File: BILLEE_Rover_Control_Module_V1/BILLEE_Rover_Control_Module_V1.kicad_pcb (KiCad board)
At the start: 4 copper layers, 240 x 90.5 mm, 276 parts, among them CN1 XT90PW-M.G.Y, CN10 XT60PW-M, CN11 XT60PW-M, CN12 XT60PW-M, CN13 XT60PW-M, CN14 XT60PW-M, CN15 XT60PW-M, CN16 XT60PW-M, CN17 XT60PW-M, CN18 XT60PW-M, CN2 XT60PW-M, CN3 XT60PW-M, CN4 XT60PW-M, CN5 XT60PW-M, CN6 DF11-18DP-2DSA, CN7 XT90PW-M.G.Y, CN8 XT90PW-M.G.Y, CN9 XT90PW-M.G.Y, J1 2.54mm Header, Q1 IPT007N06N, Q2 IPT007N06N, Q3 IPT007N06N, Q4 IPT007N06N, Q5 IPT007N06N, Q6 IPT007N06N, Q7 IPT007N06N, Q8 IPT007N06N, SW1 33uH, SW2 KMR2, SW3 RESET SW, U1 INA780BIDEKR, U10 RP2350A_C42411118, U11 ABM8-272-T3_C20625731, U12 W25Q128JVSIQTR, U13 TCA4307DGKR, U14 TCA4307DGKR, U15 TXS0108EPWR, U16 ESTOP, U17 SN74LVC08APWR, U18 SN74LVC08APWR, U19 LTC7001IMSE#PBF, U2 MCP9808T-E/MS, U20 LTC7001IMSE#PBF, U21 LTC7001IMSE#PBF, U22 LTC7001IMSE#PBF, U23 LTC7001IMSE#PBF, U24 LTC7001IMSE#PBF, U25 INA780BIDEKR, U26 INA780BIDEKR, U27 INA780BIDEKR, U28 INA780BIDEKR, U29 INA780BIDEKR, U3 TPS1HA08BQPWPRQ1, U30 INA780BIDEKR, U31 LTC7001IMSE#PBF, U32 LTC7001IMSE#PBF, U33 INA780BIDEKR, U34 INA780BIDEKR, U35 MCP9808T-E/MS, U36 MCP9808T-E/MS, U4 TPS1HA08BQPWPRQ1, U5 TPS1HA08BQPWPRQ1, U6 LT8612EUDE#TRPBF, U7 LT8612EUDE#TRPBF, U8 LT8612EUDE#TRPBF, U9 10uH

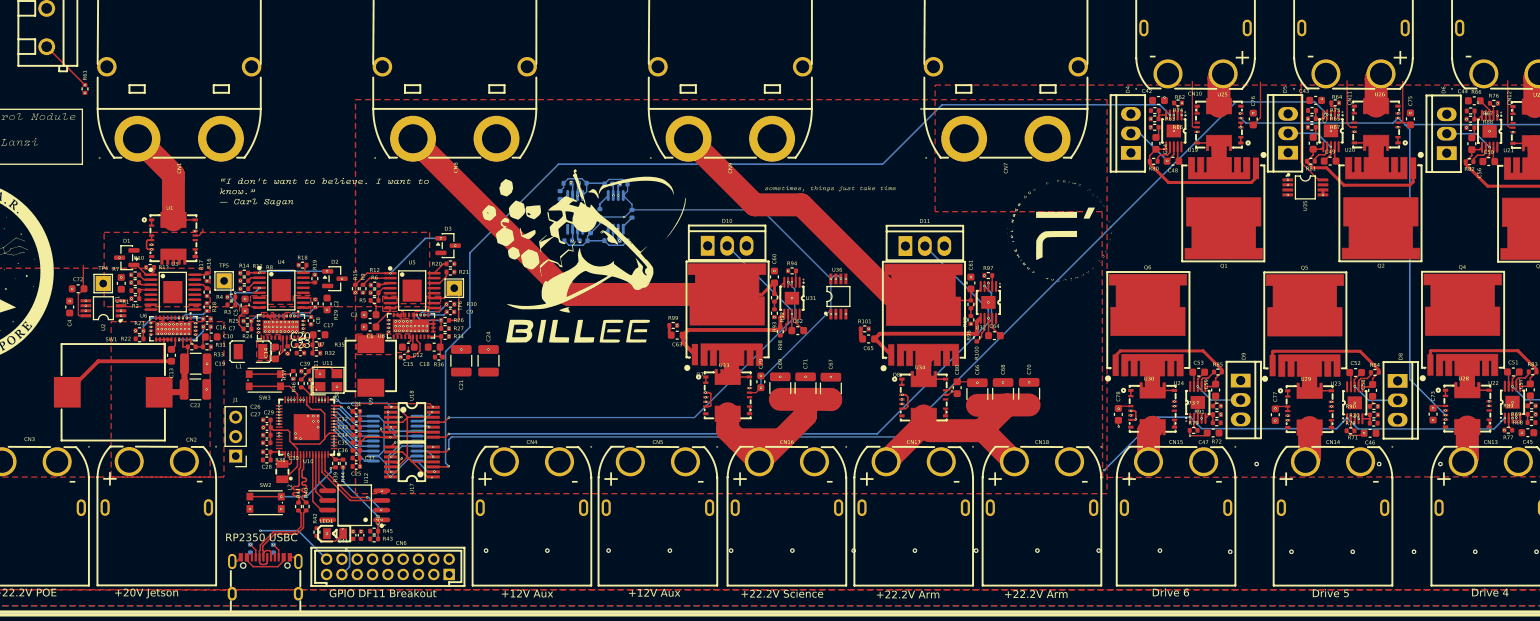
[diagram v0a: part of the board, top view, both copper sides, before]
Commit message: JLCPCB Complaint 2oz/1oz Constraints
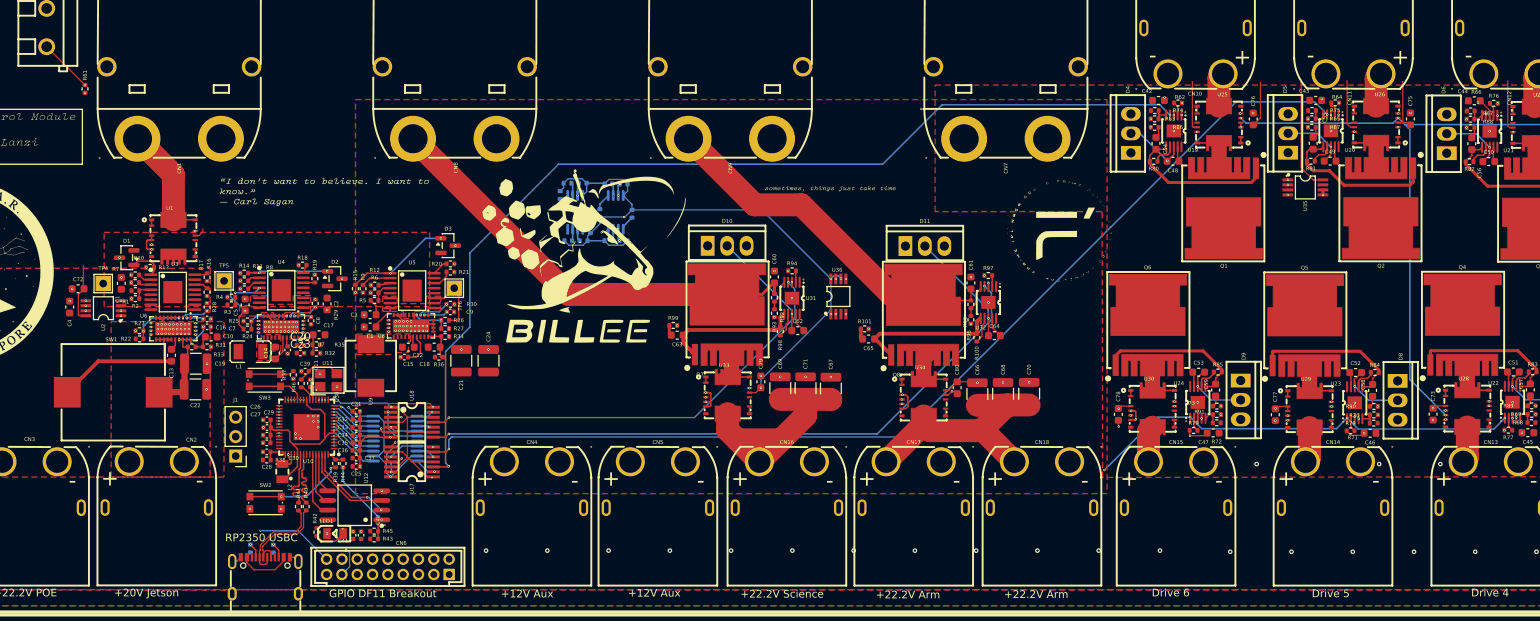
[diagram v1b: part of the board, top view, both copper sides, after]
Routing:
- net Net-(D1-A): track 3.86 -> 4.53 mm
- net VBUS_USB: track 6.31 -> 6.85 mm
